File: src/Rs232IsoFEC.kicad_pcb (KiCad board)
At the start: 2 copper layers, 24 x 27.9 mm, 22 parts, among them J1 B3B-XH-A, P1 105444-0001, U1 FT232RL, U2 ADM3251E

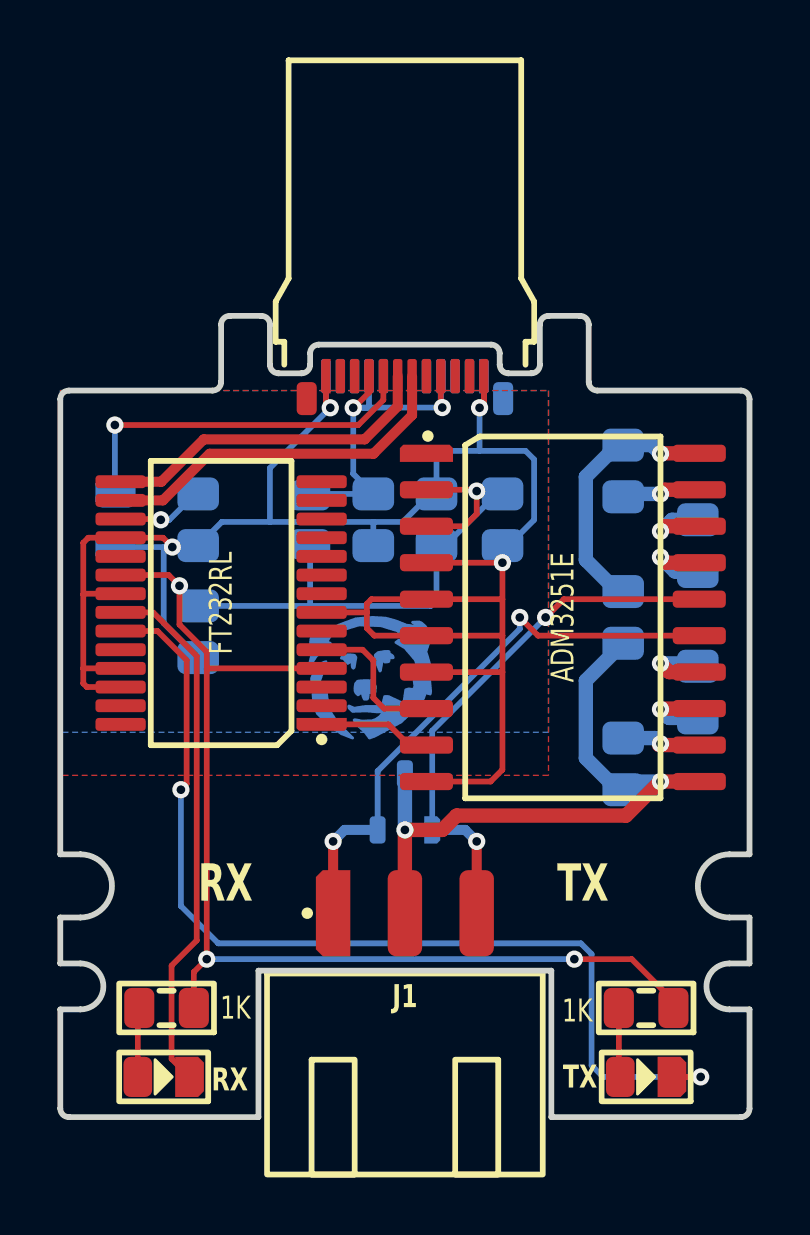
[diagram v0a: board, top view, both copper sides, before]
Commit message: Added mosfet to turn off isolator in sleep mode
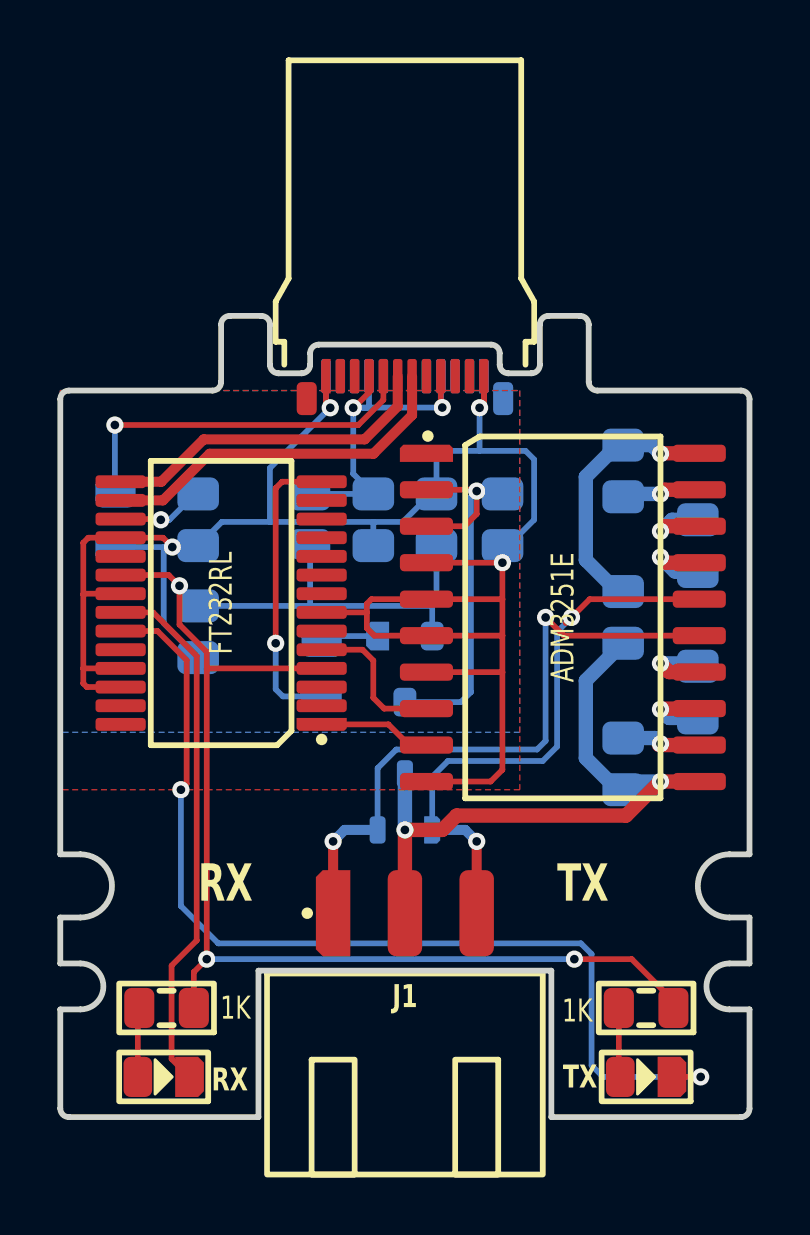
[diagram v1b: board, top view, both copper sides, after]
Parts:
- removed ICON: Medo64, Medo64:ICON Medo64
- added Q1: DMP3099L-13, Medo64:Q MOSFET-P (SOT23-3), B.Cu at (32.0, 32.3)
- added R3: 1K, Medo64:R (0805), B.Cu at (29.1, 32.3)
- renumbered R3 to R4
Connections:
- C4 pad 2: 5V -> 5V_SW
- U1 pad 14: (no net) -> PWREN#
- U2 pad 2: 5V -> 5V_SW
- U2 pad 3: 5V -> 5V_SW
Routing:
- net 5V_SW: track 0.00 -> 14.8 mm, vias 0 -> 1
- net PWREN#: track 0.00 -> 10.4 mm, vias 0 -> 1
- net 5V: track 59.8 -> 53.3 mm, vias 4 -> 3
- net ISO_RXD: track 20.2 -> 22.5 mm
- net PWREN#': track 0.00 -> 2.03 mm
- net ISO_TXD: track 18.9 -> 20.6 mm
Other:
- board text added: "Rs232IsoFEC A"
- board text removed: "Rs232IsoFEC C"

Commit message: Added soft-start capacitor for isolator
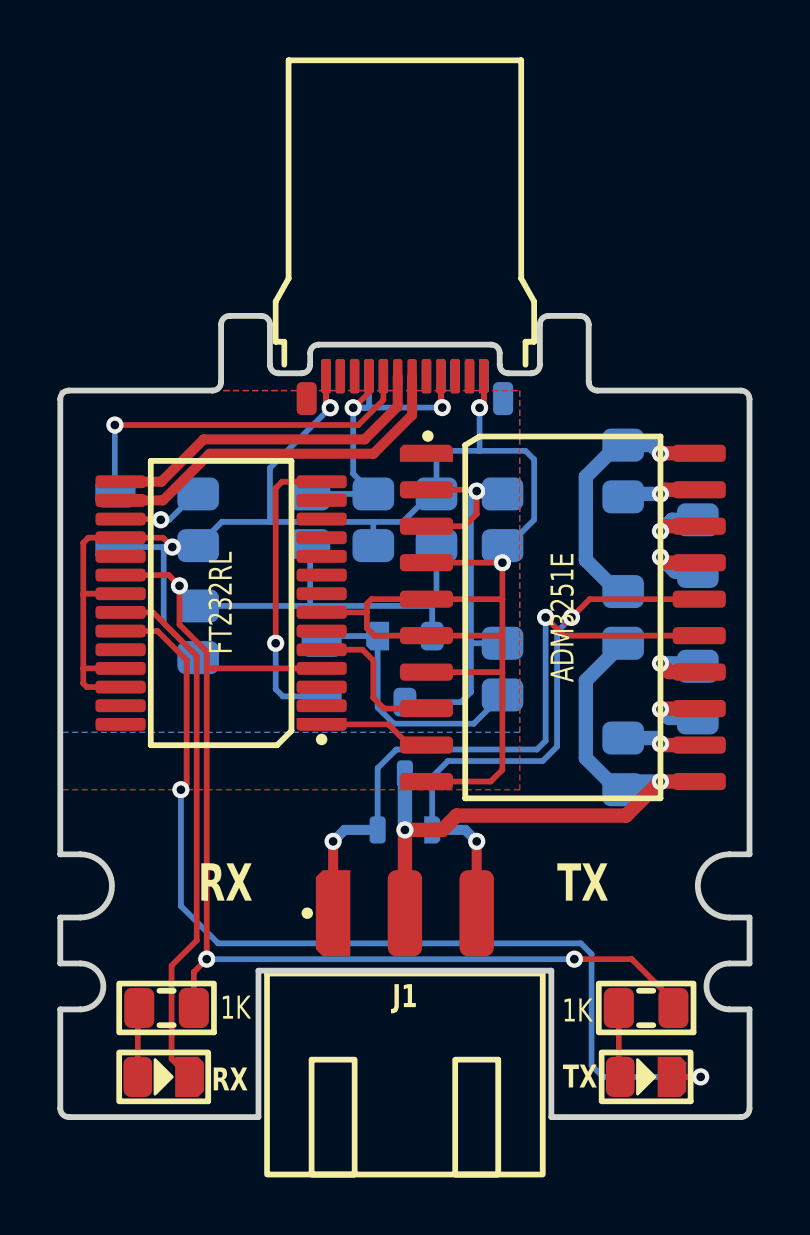
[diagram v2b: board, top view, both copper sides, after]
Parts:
- added C10: 100n, Medo64:C (0805), B.Cu at (35.4, 32.3)
- renumbered C10 to C11
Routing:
- net PWREN#': track 2.03 -> 9.52 mm
- net 5V_SW: track 14.8 -> 15.9 mm
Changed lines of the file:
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@@
     (tags "CAPC2013X140N")
     (attr smd)
-    (fp_text reference "C10" (at 0 1.6 90) (layer "B.SilkS") hide
+    (fp_text reference "C11" (at 0 1.6 90) (layer "B.SilkS") hide
         (effects (font (size 0.8 0.6) (thickness 0.15) bold) (justify mirror))
     )
@@
     (pad "2" smd roundrect (at 0.9 0 270) (size 1.15 1.45) (layers "B.Cu" "B.Paste" "B.Mask") (roundrect_rratio 0.25)
       (net 3 "5V") (thermal_bridge_angle 45))
+    (model ":KICAD7_3DMODEL_DIR:Capacitor_SMD.3dshapes/C_0805_2012Metric.step"
+      (offset (xyz 0 0 0))
+      (scale (xyz 1 1 1))
+      (rotate (xyz 0 0 0))
+    )
+  )
+  (footprint "Medo64:C (0805)" (layer "B.Cu")
+    (at 35.4 32.3 90)
+    (tags "CAPC2013X140N")
+    (attr smd)
+    (fp_text reference "C10" (at 0 1.6 90) (layer "B.SilkS") hide
+        (effects (font (size 0.8 0.6) (thickness 0.15) bold) (justify mirror))
+    )
+    (fp_text value "100n" (at -2.4 0) (layer "B.SilkS")
+        (effects (font (size 0.8 0.6) (thickness 0.15) bold) (justify mirror))
+    )
+    (fp_text user "soft-start" (at 0 0 90 unlocked) (layer "B.SilkS") hide
+        (effects (font (size 1 1) (thickness 0.1)) (justify mirror))
+    )
+    (fp_line (start 0 0.625) (end 0 -0.625)
+      (stroke (width 0.2) (type default)) (layer "B.SilkS"))
+    (fp_rect (start -1.65 0.9) (end 1.65 -0.9)
+      (stroke (width 0.2) (type default)) (fill none) (layer "B.SilkS"))
+    (fp_rect (start -1.75 1) (end 1.75 -1)
+      (stroke (width 0.01) (type dash)) (fill none) (layer "B.CrtYd"))
+    (fp_rect (start -1 0.625) (end 1 -0.625)
+      (stroke (width 0.01) (type dash_dot)) (fill none) (layer "B.Fab"))
+    (pad "1" smd roundrect (at -0.9 0 90) (size 1.15 1.45) (layers "B.Cu" "B.Paste" "B.Mask") (roundrect_rratio 0.25)
+      (net 25 "PWREN#'") (thermal_bridge_angle 45))
+    (pad "2" smd roundrect (at 0.9 0 90) (size 1.15 1.45) (layers "B.Cu" "B.Paste" "B.Mask") (roundrect_rratio 0.25)
+      (net 24 "5V_SW") (thermal_bridge_angle 45))
     (model ":KICAD7_3DMODEL_DIR:Capacitor_SMD.3dshapes/C_0805_2012Metric.step"
       (offset (xyz 0 0 0))
@@
   (via (at 34.5 26.1) (size 0.6) (drill 0.3) (layers "F.Cu" "B.Cu") (net 24))
   (segment (start 34.3 26.3) (end 34.5 26.1) (width 0.2) (layer "B.Cu") (net 24))
+  (segment (start 34.3 31.4) (end 34.3 26.3) (width 0.2) (layer "B.Cu") (net 24))
   (segment (start 32 33.45) (end 33.95 33.45) (width 0.2) (layer "B.Cu") (net 24))
   (segment (start 33.95 33.45) (end 34.3 33.1) (width 0.2) (layer "B.Cu") (net 24))
-  (segment (start 34.3 33.1) (end 34.3 26.3) (width 0.2) (layer "B.Cu") (net 24))
+  (segment (start 34.3 33.1) (end 34.3 31.4) (width 0.2) (layer "B.Cu") (net 24))
+  (segment (start 35.4 31.4) (end 34.3 31.4) (width 0.2) (layer "B.Cu") (net 24))
   (segment (start 34.5 26.1) (end 35.3 26.1) (width 0.2) (layer "B.Cu") (net 24))
   (segment (start 31.05 31.15) (end 29.3 31.15) (width 0.2) (layer "B.Cu") (net 25))
+  (segment (start 34.4 34.2) (end 31.613604 34.2) (width 0.2) (layer "B.Cu") (net 25))
+  (segment (start 31.613604 34.2) (end 31.05 33.636396) (width 0.2) (layer "B.Cu") (net 25))
+  (segment (start 31.05 33.636396) (end 31.05 31.15) (width 0.2) (layer "B.Cu") (net 25))
   (segment (start 29.3 31.15) (end 29.1 31.35) (width 0.2) (layer "B.Cu") (net 25))
+  (segment (start 35.4 33.2) (end 34.4 34.2) (width 0.2) (layer "B.Cu") (net 25))
   (segment (start 27.5 26) (end 27.5 31.4) (width 0.2) (layer "F.Cu") (net 26))
   (segment (start 27.725 25.775) (end 27.5 26) (width 0.2) (layer "F.Cu") (net 26))

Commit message: Updated protection diode to 12V
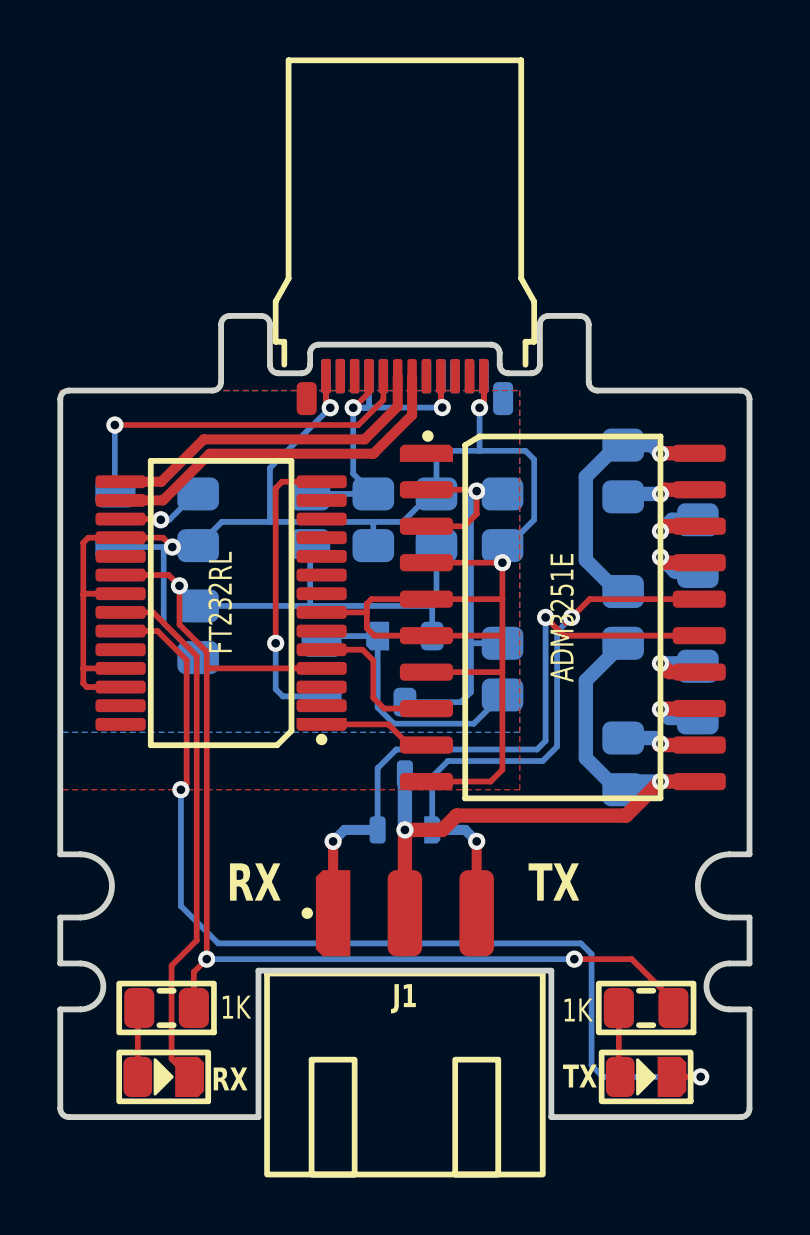
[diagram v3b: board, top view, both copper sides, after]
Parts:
- D1: value SM05T1G -> SM12T1G
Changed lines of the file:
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@@
         (effects (font (size 0.8 0.6) (thickness 0.15)) (justify mirror))
     )
-    (fp_text value "SM05T1G" (at 0 -2.2) (layer "B.SilkS") hide
-        (effects (font (size 0.8 0.6) (thickness 0.15)) (justify mirror))
-    )
-    (fp_text user "C" (at -0.95 -0.4) (layer "Cmts.User" knockout)
+    (fp_text value "SM12T1G" (at 0 -2.2) (layer "B.SilkS") hide
+        (effects (font (size 0.8 0.6) (thickness 0.15)) (justify mirror))
+    )
+    (fp_text user "C" (at 0.95 -0.4) (layer "Cmts.User" knockout)
         (effects (font (size 0.13 0.07) (thickness 0.01) bold))
     )
@@
         (effects (font (size 0.13 0.07) (thickness 0.01) bold))
     )
-    (fp_text user "C" (at 0.95 -0.4) (layer "Cmts.User" knockout)
+    (fp_text user "C" (at -0.95 -0.4) (layer "Cmts.User" knockout)
         (effects (font (size 0.13 0.07) (thickness 0.01) bold))
     )
@@
     (effects (font (size 0.8 0.6) (thickness 0.15) bold) (justify mirror))
   )
-  (gr_text "RX" (at 26.7 39) (layer "F.SilkS" knockout)
+  (gr_text "RX" (at 27.7 39) (layer "F.SilkS" knockout)
     (effects (font (size 1.3 0.9) (thickness 0.15) bold) (justify right top))
   )
-  (gr_text "TX" (at 37.3 39) (layer "F.SilkS" knockout)
+  (gr_text "TX" (at 36.3 39) (layer "F.SilkS" knockout)
     (effects (font (size 1.3 0.9) (thickness 0.15) bold) (justify left top))
   )

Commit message: Added RTS/CTS loopback
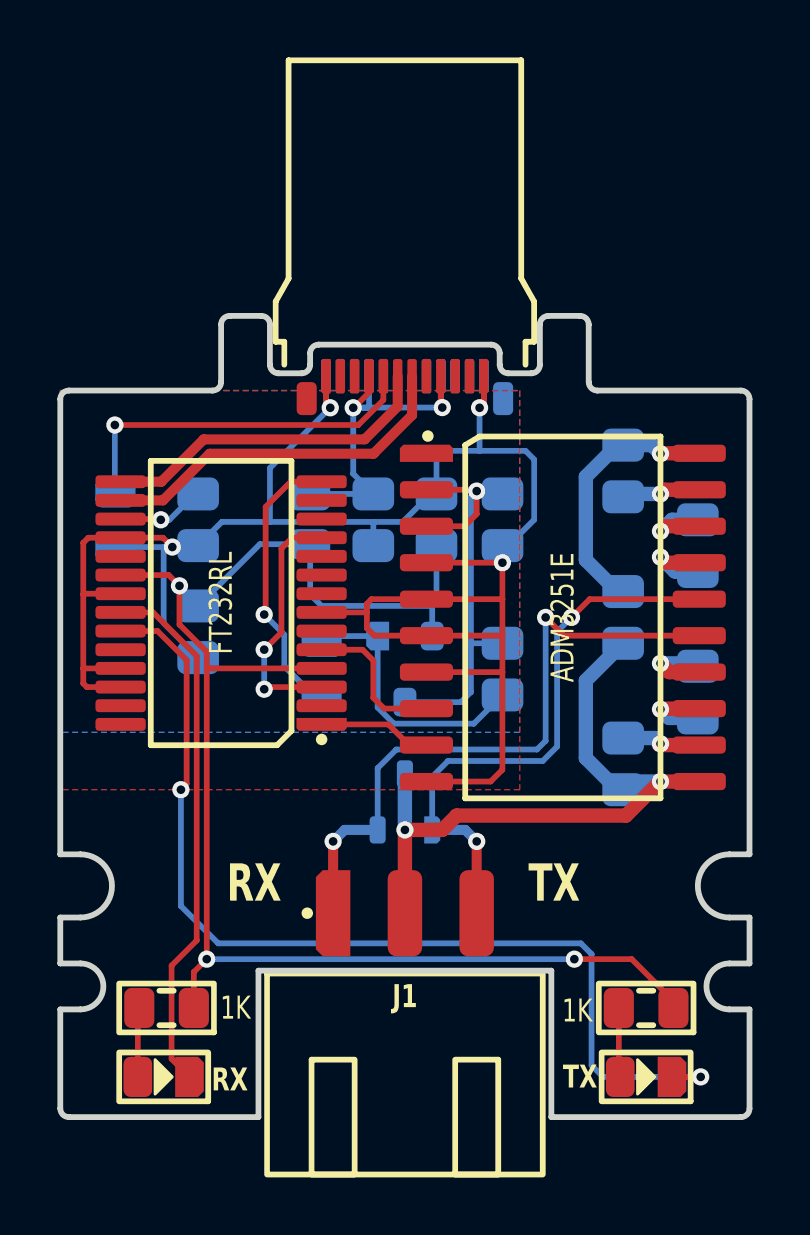
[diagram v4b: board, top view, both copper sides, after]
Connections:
- U1 pad 11: (no net) -> RTS_CTS
- U1 pad 3: (no net) -> RTS_CTS
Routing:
- net RTS_CTS: track 0.00 -> 8.73 mm, vias 0 -> 2
- net PWREN#: track 10.4 -> 9.66 mm
- net 5V: track 53.3 -> 53.9 mm
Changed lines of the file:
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@@
   (net 25 "PWREN#'")
   (net 26 "PWREN#")
+  (net 27 "RTS_CTS")
   (footprint "Medo64:R (0805)" (layer "F.Cu")
     (at 40.4 44.1 180)
@@
       (thermal_bridge_angle 45))
     (pad "3" smd roundrect (at -3.5 -2.925 180) (size 1.75 0.45) (layers "F.Cu" "F.Paste" "F.Mask") (roundrect_rratio 0.25)
-      (thermal_bridge_angle 45))
+      (net 27 "RTS_CTS") (thermal_bridge_angle 45))
     (pad "4" smd roundrect (at -3.5 -2.275 180) (size 1.75 0.45) (layers "F.Cu" "F.Paste" "F.Mask") (roundrect_rratio 0.25)
       (net 3 "5V") (thermal_bridge_angle 45))
@@
       (thermal_bridge_angle 45))
     (pad "11" smd roundrect (at -3.5 2.275 180) (size 1.75 0.45) (layers "F.Cu" "F.Paste" "F.Mask") (roundrect_rratio 0.25)
-      (thermal_bridge_angle 45))
+      (net 27 "RTS_CTS") (thermal_bridge_angle 45))
     (pad "12" smd roundrect (at -3.5 2.925 180) (size 1.75 0.45) (layers "F.Cu" "F.Paste" "F.Mask") (roundrect_rratio 0.25)
       (thermal_bridge_angle 45))
@@
   (via (at 25.099647 42.399647) (size 0.6) (drill 0.3) (layers "F.Cu" "B.Cu") (net 3))
   (segment (start 25.099647 42.399647) (end 25.1 42.4) (width 0.2) (layer "B.Cu") (net 3))
+  (segment (start 28.7 29.7) (end 28.7 29.1) (width 0.2) (layer "B.Cu") (net 3))
+  (segment (start 33.1 29.9) (end 32.9 30.1) (width 0.2) (layer "B.Cu") (net 3))
   (segment (start 24.8 30.1) (end 24.15 29.45) (width 0.2) (layer "B.Cu") (net 3))
   (segment (start 32.95 30.05) (end 33.1 29.9) (width 0.2) (layer "B.Cu") (net 3))
-  (segment (start 33.1 29.9) (end 32.9 30.1) (width 0.2) (layer "B.Cu") (net 3))
-  (segment (start 32.9 30.1) (end 28.7 30.1) (width 0.2) (layer "B.Cu") (net 3))
-  (segment (start 28.7 30.1) (end 28.7 27.95) (width 0.2) (layer "B.Cu") (net 3))
+  (segment (start 29.1 30.1) (end 28.7 29.7) (width 0.2) (layer "B.Cu") (net 3))
+  (segment (start 32.9 30.1) (end 29.1 30.1) (width 0.2) (layer "B.Cu") (net 3))
+  (segment (start 26.95 27.95) (end 24.8 30.1) (width 0.2) (layer "B.Cu") (net 3))
   (segment (start 24.15 29.45) (end 24.15 29.4) (width 0.2) (layer "B.Cu") (net 3))
   (segment (start 25.1 42.4) (end 37.899988 42.4) (width 0.2) (layer "B.Cu") (net 3))
   (segment (start 32.95 31.15) (end 32.95 30.05) (width 0.2) (layer "B.Cu") (net 3))
   (segment (start 33.1 28) (end 33.1 29.9) (width 0.2) (layer "B.Cu") (net 3))
-  (segment (start 24.8 30.1) (end 28.7 30.1) (width 0.2) (layer "B.Cu") (net 3))
+  (segment (start 28.7 27.95) (end 26.95 27.95) (width 0.2) (layer "B.Cu") (net 3))
+  (segment (start 28.7 29.1) (end 28.7 27.95) (width 0.2) (layer "B.Cu") (net 3))
   (segment (start 30.9 33.3) (end 30.9 32) (width 0.2) (layer "F.Cu") (net 4))
   (segment (start 30.9 32) (end 30.525 31.625) (width 0.2) (layer "F.Cu") (net 4))
@@
   (segment (start 36.6 35.1) (end 36.9 34.8) (width 0.2) (layer "B.Cu") (net 15))
   (segment (start 31.05 37.9) (end 31.05 35.75) (width 0.2) (layer "B.Cu") (net 15))
-  (segment (start 37.8 30.5) (end 37.6 30.7) (width 0.2) (layer "F.Cu") (net 16))
   (segment (start 42.25 29.865) (end 38.435 29.865) (width 0.2) (layer "F.Cu") (net 16))
   (segment (start 38.435 29.865) (end 37.8 30.5) (width 0.2) (layer "F.Cu") (net 16))
@@
   (segment (start 31.613604 34.2) (end 31.05 33.636396) (width 0.2) (layer "B.Cu") (net 25))
   (segment (start 31.05 33.636396) (end 31.05 31.15) (width 0.2) (layer "B.Cu") (net 25))
-  (segment (start 29.3 31.15) (end 29.1 31.35) (width 0.2) (layer "B.Cu") (net 25))
   (segment (start 35.4 33.2) (end 34.4 34.2) (width 0.2) (layer "B.Cu") (net 25))
-  (segment (start 27.5 26) (end 27.5 31.4) (width 0.2) (layer "F.Cu") (net 26))
-  (segment (start 27.725 25.775) (end 27.5 26) (width 0.2) (layer "F.Cu") (net 26))
-  (segment (start 29.1 25.775) (end 27.725 25.775) (width 0.2) (layer "F.Cu") (net 26))
-  (via (at 27.5 31.4) (size 0.6) (drill 0.3) (layers "F.Cu" "B.Cu") (net 26))
-  (segment (start 27.5 33) (end 27.75 33.25) (width 0.2) (layer "B.Cu") (net 26))
-  (segment (start 27.5 31.4) (end 27.5 33) (width 0.2) (layer "B.Cu") (net 26))
-  (segment (start 27.75 33.25) (end 29.1 33.25) (width 0.2) (layer "B.Cu") (net 26))
+  (segment (start 27.15 26.65) (end 27.15 30.349996) (width 0.2) (layer "F.Cu") (net 26))
+  (segment (start 28.025 25.775) (end 27.15 26.65) (width 0.2) (layer "F.Cu") (net 26))
+  (segment (start 29.1 25.775) (end 28.025 25.775) (width 0.2) (layer "F.Cu") (net 26))
+  (segment (start 27.15 30.349996) (end 27.1 30.399996) (width 0.2) (layer "F.Cu") (net 26))
+  (via (at 27.1 30.399996) (size 0.6) (drill 0.3) (layers "F.Cu" "B.Cu") (net 26))
+  (segment (start 28.85 33.25) (end 27.8 32.2) (width 0.2) (layer "B.Cu") (net 26))
+  (segment (start 27.8 31.099996) (end 27.1 30.399996) (width 0.2) (layer "B.Cu") (net 26))
+  (segment (start 27.8 32.2) (end 27.8 31.099996) (width 0.2) (layer "B.Cu") (net 26))
+  (segment (start 29.1 27.725) (end 28.075 27.725) (width 0.2) (layer "F.Cu") (net 27))
+  (segment (start 27.7 28.1) (end 27.7 31.022198) (width 0.2) (layer "F.Cu") (net 27))
+  (segment (start 28.075 27.725) (end 27.7 28.1) (width 0.2) (layer "F.Cu") (net 27))
+  (segment (start 27.7 31.022198) (end 27.1 31.622198) (width 0.2) (layer "F.Cu") (net 27))
+  (segment (start 27.175 32.925) (end 27.1 33) (width 0.2) (layer "F.Cu") (net 27))
+  (segment (start 29.1 32.925) (end 27.175 32.925) (width 0.2) (layer "F.Cu") (net 27))
+  (via (at 27.1 31.622198) (size 0.6) (drill 0.3) (layers "F.Cu" "B.Cu") (net 27))
+  (via (at 27.1 33) (size 0.6) (drill 0.3) (layers "F.Cu" "B.Cu") (net 27))
+  (segment (start 27.1 33) (end 27.1 31.622198) (width 0.2) (layer "B.Cu") (net 27))
   (zone (net 7) (net_name "GND") (layer "F.Cu") (hatch edge 0.5)
     (connect_pads (clearance 0.35))
